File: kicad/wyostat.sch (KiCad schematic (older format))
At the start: 83 parts, among them J1 24 V AC IN, J10 Y2, J11 G, J12 W1, J13 USB_microAB, J14 W2, J15 Conn_Spare, J16 5V_SEL, J2 OUT1, J3 OUT2, J4 OUT3, J5 I2C_ext1, J6 RH, J7 RC, J8 C, J9 Y1, Q1 BTA204S, Q2 BTA204S, Q3 BTA204S, U1 MOC3063M, U2 MOC3063M, U3 MOC3063M, U4 Wemos-Lolin, U5 MAX17502FATB+T

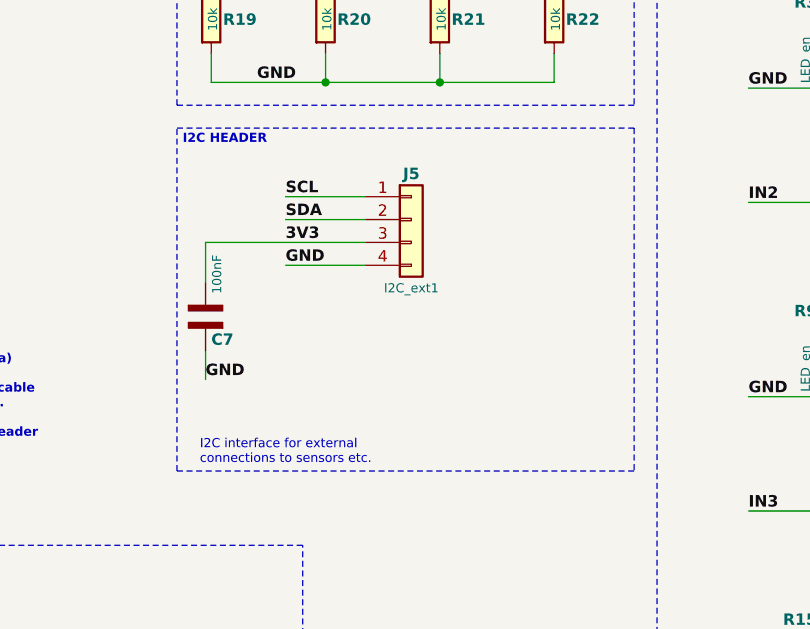
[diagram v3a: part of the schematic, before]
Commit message: added Sparkfun TMP102 footprint and PCB edges modified
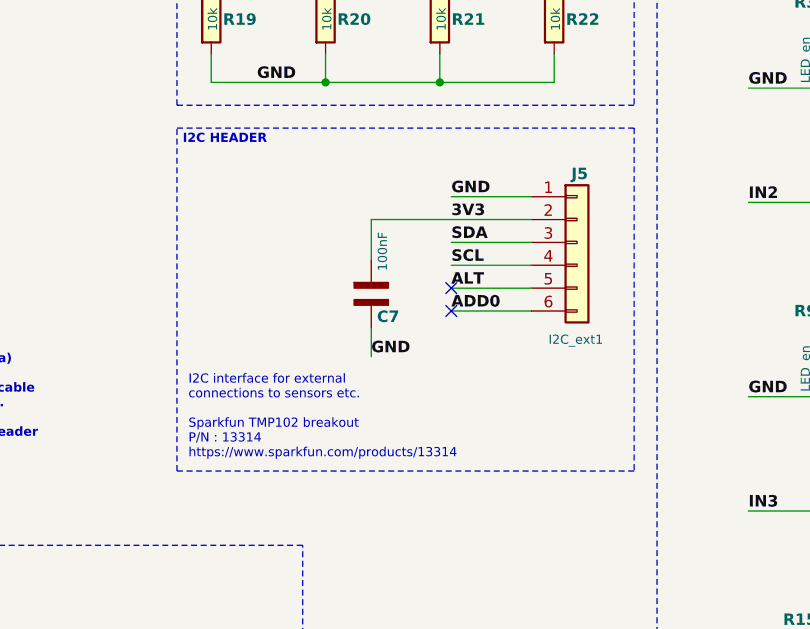
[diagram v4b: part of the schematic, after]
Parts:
- removed J5: I2C_ext1, wyostat_fp:Pin_Header_Straight_1x04, symbol wyostat:Conn_01x04
- added J5: I2C_ext1, wyostat_fp:Pin_Header_TMP102_1x06, symbol wyostat:Conn_01x06
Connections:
- net 3V3: now also J5.2 (Pin_2)
- net GND: now also J5.1 (Pin_1)
- net SCL: now also J5.4 (Pin_4)
- net SDA: now also J5.3 (Pin_3)
- new net ADD0: J5.6 (Pin_6)
- new net ALT: J5.5 (Pin_5)
- no-connect marks 15 -> 17
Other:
- note added: "I2C interface for external\nconnections to sensors etc.\n\nSparkfun TMP102 breakout\nP/N : 13314\nhttps://www.sparkfun.com/products/13314"
- note removed: "I2C interface for external\nconnections to sensors etc.\n"
- moved on the sheet: C7
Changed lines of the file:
@@
 Wire Notes Line
 	4825 2075 4825 575
-$Comp
-L wyostat:Conn_01x04 J5
-U 1 1 5AA95913
-P 5850 2575
-F 0 "J5" H 5850 2775 50  0000 C CNB
-F 1 "I2C_ext1" H 5850 2275 40  0000 C CNN
-F 2 "wyostat_fp:Pin_Header_Straight_1x04" H 5850 2575 50  0001 C CNN
-F 3 "~" H 5850 2575 50  0001 C CNN
-	1    5850 2575
-	1    0    0    -1
-$EndComp
-Text Label 5300 2575 0    50   ~ 10
+Text Label 6025 2675 0    50   ~ 10
 SDA
-Text Label 5300 2475 0    50   ~ 10
+Text Label 6025 2775 0    50   ~ 10
 SCL
-Text Label 5300 2675 0    50   ~ 10
+Text Label 6025 2575 0    50   ~ 10
 3V3
-Text Label 5300 2775 0    50   ~ 10
+Text Label 6025 2475 0    50   ~ 10
 GND
 Wire Wire Line
-	5650 2475 5300 2475
+	6375 2775 6025 2775
 Wire Wire Line
-	5300 2575 5650 2575
+	6025 2675 6375 2675
 Wire Wire Line
-	5300 2775 5650 2775
-Text Notes 4925 3650 0    40   ~ 0
-I2C interface for external\nconnections to sensors etc.\n
+	6025 2475 6375 2475
+Text Notes 4875 3625 0    40   ~ 0
+I2C interface for external\nconnections to sensors etc.\n\nSparkfun TMP102 breakout\nP/N : 13314\nhttps://www.sparkfun.com/products/13314
 Wire Notes Line
 	4825 2175 6825 2175
@@
 L wyostat:C_NP C7
 U 1 1 5AA95948
-P 4950 3000
-F 0 "C7" H 4975 2900 50  0000 L CNB
-F 1 "100nF" V 5000 3100 40  0000 L CNN
-F 2 "wyostat_fp:C_0805" H 4950 3000 60  0001 C CNN
-F 3 "" H 4950 3000 60  0000 C CNN
-	1    4950 3000
+P 5675 2900
+F 0 "C7" H 5700 2800 50  0000 L CNB
+F 1 "100nF" V 5725 3000 40  0000 L CNN
+F 2 "wyostat_fp:C_0805" H 5675 2900 60  0001 C CNN
+F 3 "" H 5675 2900 60  0000 C CNN
+	1    5675 2900
 	1    0    0    -1
 $EndComp
 Wire Wire Line
-	4950 2675 4950 2850
+	5675 2575 5675 2750
 Wire Wire Line
-	4950 2675 5650 2675
+	5675 2575 6375 2575
 Wire Wire Line
-	4950 3150 4950 3275
-Text Label 4950 3275 0    50   ~ 10
+	5675 3050 5675 3175
+Text Label 5675 3175 0    50   ~ 10
 GND
 Connection ~ 7675 1150
@@
 Text Notes 9475 5425 0    40   ~ 0
 Extra connection pads\nbrokenout to screw connector
+$Comp
+L wyostat:Conn_01x06 J5
+U 1 1 5ACA4E5A
+P 6575 2675
+F 0 "J5" H 6550 2975 50  0000 L CNB
+F 1 "I2C_ext1" H 6450 2250 40  0000 L CNN
+F 2 "wyostat_fp:Pin_Header_TMP102_1x06" H 6575 2675 50  0001 C CNN
+F 3 "~" H 6575 2675 50  0001 C CNN
+	1    6575 2675
+	1    0    0    -1
+$EndComp
+Wire Wire Line
+	6375 2875 6025 2875
+Wire Wire Line
+	6375 2975 6025 2975
+Text Label 6025 2875 0    50   ~ 10
+ALT
+Text Label 6025 2975 0    50   ~ 10
+ADD0
+NoConn ~ 6025 2875
+NoConn ~ 6025 2975
 $EndSCHEMATC

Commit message: prettified silk legend
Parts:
- C11: symbol wyostat:C_POL -> wyostat:C_NP
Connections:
- net 24Vac-H: now also C1.2 (-), C3.2 (-), C5.2 (-), R1.2, R13.2, R7.2; no longer C1.1 (+), C3.1 (+), C5.1 (+), R1.1, R13.1, R7.1
- net 3V3: now also C7.2 (-), S4.2, S4.4; no longer C7.1 (+), S4.1, S4.3
- net 40VDC: now also C11.2 (-); no longer C11.1 (+)
- net 5V_USB: now also L2.1; no longer L2.2
- net GND: now also C11.1 (+), C13.1 (+), C7.1 (+), JP1.2, JP2.2, JP3.2; no longer C11.2 (-), C13.2 (-), C7.2 (-), JP1.1, JP2.1, JP3.1
- net OUT1: now also R5.2; no longer R5.1
- net OUT2: now also R12.2; no longer R12.1
- net OUT3: now also R17.2; no longer R17.1
- net SS: now also C13.2 (-); no longer C13.1 (+)
- net SW_M: now also S4.1, S4.3; no longer S4.2, S4.4
- net USB+: now also L2.2; no longer L2.1
- net at Q1.3 (G), U1.4: now also R5.1; no longer R5.2
- net at U1.6: now also R1.1; no longer R1.2
- net at R3.1: now also JP1.1; no longer JP1.2
- net at Q2.3 (G), U2.4: now also R12.1; no longer R12.2
- net at U2.6: now also R7.1; no longer R7.2
- net at R9.1: now also JP2.1; no longer JP2.2
- net at Q3.3 (G), U3.4: now also R17.1; no longer R17.2
- net at U3.6: now also R13.1; no longer R13.2
- net at R15.1: now also JP3.1; no longer JP3.2
- net at R6.2: now also C1.1 (+); no longer C1.2 (-)
- net at R11.2: now also C3.1 (+); no longer C3.2 (-)
- net at R18.2: now also C5.1 (+); no longer C5.2 (-)
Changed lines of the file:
@@
 F 4 "Value" H 8775 1150 50  0001 C CNN "manf#"
 	1    8775 1150
-	0    1    1    0
+	0    -1   1    0
 $EndComp
 Text Label 10325 2025 0    50   ~ 10
@@
 F 4 "Value" H 8775 2500 50  0001 C CNN "manf#"
 	1    8775 2500
-	0    1    1    0
+	0    -1   1    0
 $EndComp
 Text Label 10325 3375 0    50   ~ 10
@@
 F 4 "Value" H 8775 3850 50  0001 C CNN "manf#"
 	1    8775 3850
-	0    1    1    0
+	0    -1   1    0
 $EndComp
 Text Label 10325 4725 0    50   ~ 10
@@
 U 1 1 5AA957F2
 P 6525 1125
-F 0 "S4" V 6600 1250 50  0000 L CNB
+F 0 "S4" V 6450 1250 50  0000 L CNB
 F 1 "SW-MODE" H 6525 1025 40  0000 C CNN
 F 2 "wyostat_fp:SW_SPST_FSM6JSMA" H 6525 1125 60  0001 C CNN
 F 3 "" H 6525 1125 60  0000 C CNN
 	1    6525 1125
-	0    1    1    0
+	0    1    -1   0
 $EndComp
 Wire Wire Line
@@
 P 5675 2900
 F 0 "C7" H 5700 2800 50  0000 L CNB
-F 1 "100nF" V 5725 3000 40  0000 L CNN
+F 1 "100nF" V 5625 2625 40  0000 L CNN
 F 2 "wyostat_fp:C_0805" H 5675 2900 60  0001 C CNN
 F 3 "" H 5675 2900 60  0000 C CNN
 	1    5675 2900
-	1    0    0    -1
+	1    0    0    1
 $EndComp
 Wire Wire Line
@@
 P 7675 1900
 F 0 "JP1" V 7675 1875 50  0000 R CNB
-F 1 "LED_en" H 7800 2000 40  0000 R CNN
+F 1 "LED_en" H 7775 2000 40  0000 R CNN
 F 2 "wyostat_fp:R_0805" H 7675 1900 50  0001 C CNN
 F 3 "" H 7675 1900 50  0001 C CNN
 	1    7675 1900
-	0    -1   -1   0
+	0    -1   1    0
 $EndComp
 Wire Wire Line
@@
 P 7675 3250
 F 0 "JP2" V 7675 3225 50  0000 R CNB
-F 1 "LED_en" H 7800 3350 40  0000 R CNN
+F 1 "LED_en" H 7750 3350 40  0000 R CNN
 F 2 "wyostat_fp:R_0805" H 7675 3250 50  0001 C CNN
 F 3 "" H 7675 3250 50  0001 C CNN
 	1    7675 3250
-	0    -1   -1   0
+	0    -1   1    0
 $EndComp
 Connection ~ 7675 3350
@@
 P 7675 4600
 F 0 "JP3" V 7675 4575 50  0000 R CNB
-F 1 "LED_en" H 7800 4700 40  0000 R CNN
+F 1 "LED_en" H 7750 4700 40  0000 R CNN
 F 2 "wyostat_fp:R_0805" H 7675 4600 50  0001 C CNN
 F 3 "" H 7675 4600 50  0001 C CNN
 	1    7675 4600
-	0    -1   -1   0
+	0    -1   1    0
 $EndComp
 Connection ~ 7675 4700
@@
 F 5 "-" V 8850 1750 30  0001 C CNN "DNP"
 	1    8775 1750
-	-1   0    0    1
+	-1   0    0    -1
 $EndComp
 Wire Wire Line
@@
 F 5 "-" V 8850 3150 30  0001 C CNN "DNP"
 	1    8775 3150
-	-1   0    0    1
+	-1   0    0    -1
 $EndComp
 $Comp
@@
 F 5 "-" V 8850 4450 30  0001 C CNN "DNP"
 	1    8775 4450
-	-1   0    0    1
+	-1   0    0    -1
 $EndComp
 $Comp
@@
 U 1 1 5ADF342F
 P 9900 1400
-F 0 "C1" H 9925 1500 50  0000 L CNB
-F 1 "10nF,120V" H 9925 1300 40  0000 L CNN
+F 0 "C1" H 9925 1300 50  0000 L CNB
+F 1 "10nF,120V" H 9925 1500 40  0000 L CNN
 F 2 "wyostat_fp:C_1210" H 9900 1400 60  0001 C CNN
 F 3 "" H 9900 1400 60  0000 C CNN
 	1    9900 1400
-	1    0    0    -1
+	1    0    0    1
 $EndComp
 $Comp
@@
 U 1 1 5AE133E2
 P 9900 2750
-F 0 "C3" H 9925 2850 50  0000 L CNB
-F 1 "10nF,120V" H 9925 2650 40  0000 L CNN
+F 0 "C3" H 9925 2650 50  0000 L CNB
+F 1 "10nF,120V" H 9925 2850 40  0000 L CNN
 F 2 "wyostat_fp:C_1210" H 9900 2750 60  0001 C CNN
 F 3 "" H 9900 2750 60  0000 C CNN
 	1    9900 2750
-	1    0    0    -1
+	1    0    0    1
 $EndComp
 $Comp
@@
 U 1 1 5AE1E610
 P 9900 4100
-F 0 "C5" H 9925 4200 50  0000 L CNB
-F 1 "10nF,120V" H 9925 4000 40  0000 L CNN
+F 0 "C5" H 9925 4000 50  0000 L CNB
+F 1 "10nF,120V" H 9925 4200 40  0000 L CNN
 F 2 "wyostat_fp:C_1210" H 9900 4100 60  0001 C CNN
 F 3 "" H 9900 4100 60  0000 C CNN
 	1    9900 4100
-	1    0    0    -1
+	1    0    0    1
 $EndComp
 $Comp
@@
 $EndComp
 $Comp
-L wyostat:C_POL C11
+L wyostat:C_NP C11
 U 1 1 5AAA90E7
 P 2525 7075
-F 0 "C11" H 2550 6975 50  0000 L CNB
-F 1 "2.2uF,50V" V 2575 7200 40  0000 L CNN
+F 0 "C11" H 2550 7175 50  0000 L CNB
+F 1 "2.2uF,50V" V 2575 6700 40  0000 L CNN
 F 2 "wyostat_fp:C_0805" H 2525 7075 60  0001 C CNN
 F 3 "" H 2525 7075 60  0000 C CNN
 	1    2525 7075
-	1    0    0    -1
+	1    0    0    1
 $EndComp
 Wire Wire Line
@@
 U 1 1 5AB290FF
 P 2975 7075
-F 0 "C13" H 3000 6975 50  0000 L CNB
-F 1 "3.3nF" V 3025 7150 40  0000 L CNN
+F 0 "C13" H 3000 7175 50  0000 L CNB
+F 1 "3.3nF" V 2925 6825 40  0000 L CNN
 F 2 "wyostat_fp:C_0805" H 2975 7075 60  0001 C CNN
 F 3 "" H 2975 7075 60  0000 C CNN
 	1    2975 7075
-	1    0    0    -1
+	1    0    0    1
 $EndComp
 Wire Wire Line
@@
 GND
 $Comp
-L wyostat:GND #PWR02
+L wyostat:GND #PWR?
 U 1 1 5ABB9ABE
 P 2075 7600
-F 0 "#PWR02" H 2075 7350 50  0001 C CNN
+F 0 "#PWR?" H 2075 7350 50  0001 C CNN
 F 1 "GND" H 2175 7650 40  0000 C CNN
 F 2 "" H 2075 7600 50  0001 C CNN
@@
 $EndComp
 $Comp
-L wyostat:GNDREF #PWR03
+L wyostat:GNDREF #PWR?
 U 1 1 5ABDBAC8
 P 5100 7500
-F 0 "#PWR03" H 5100 7250 50  0001 C CNN
+F 0 "#PWR?" H 5100 7250 50  0001 C CNN
 F 1 "GNDREF" H 5225 7500 40  0000 C CNN
 F 2 "" H 5100 7500 50  0001 C CNN
@@
 AC-DC POWER SUPPLY
 $Comp
-L wyostat:GND #PWR01
+L wyostat:GND #PWR?
 U 1 1 5ADAE2BA
 P 3725 7375
-F 0 "#PWR01" H 3725 7125 50  0001 C CNN
+F 0 "#PWR?" H 3725 7125 50  0001 C CNN
 F 1 "GND" H 3825 7375 40  0000 C CNN
 F 2 "" H 3725 7375 50  0001 C CNN
@@
 NoConn ~ 1275 1250
 $Comp
-L wyostat:PWR_FLAG #FLG03
+L wyostat:PWR_FLAG #FLG?
 U 1 1 5AECC9F1
 P 4975 6225
-F 0 "#FLG03" H 4975 6300 50  0001 C CNN
+F 0 "#FLG?" H 4975 6300 50  0001 C CNN
 F 1 "PWR_FLAG" H 4975 6375 40  0000 C CNN
 F 2 "" H 4975 6225 50  0001 C CNN
@@
 	4975 6225 4975 6275
 $Comp
-L wyostat:PWR_FLAG #FLG01
+L wyostat:PWR_FLAG #FLG?
 U 1 1 5AEE02D5
 P 2475 775
-F 0 "#FLG01" H 2475 850 50  0001 C CNN
+F 0 "#FLG?" H 2475 850 50  0001 C CNN
 F 1 "PWR_FLAG" H 2475 925 40  0000 C CNN
 F 2 "" H 2475 775 50  0001 C CNN
@@
 Connection ~ 2475 825
 $Comp
-L wyostat:PWR_FLAG #FLG02
+L wyostat:PWR_FLAG #FLG?
 U 1 1 5AEF4507
 P 2775 775
-F 0 "#FLG02" H 2775 850 50  0001 C CNN
+F 0 "#FLG?" H 2775 850 50  0001 C CNN
 F 1 "PWR_FLAG" H 2775 925 40  0000 C CNN
 F 2 "" H 2775 775 50  0001 C CNN
@@
 U 1 1 5AE9DEF9
 P 2750 7475
-F 0 "JP4" V 2705 7552 50  0000 L CNB
-F 1 "GND" V 2795 7552 40  0000 L CNN
+F 0 "JP4" V 2775 7550 50  0000 L CNB
+F 1 "GND" V 2700 7550 40  0000 L CNN
 F 2 "wyostat_fp:LED_0402" H 2750 7475 50  0001 C CNN
 F 3 "" H 2750 7475 50  0001 C CNN
 	1    2750 7475
-	0    1    1    0
+	0    1    -1   0
 $EndComp
 Wire Wire Line
@@
 	1    0    0    -1
 $EndComp
-Wire Wire Line
-	2675 7550 2675 7400
-Wire Wire Line
-	2675 7400 2750 7325
-Wire Wire Line
-	2675 7550 2750 7625
 Text Label 675  6575 0    50   ~ 10
 24Vac-H
@@
 F 4 "Value" H 2950 4425 50  0001 C CNN "manf#"
 	1    2950 4425
-	1    0    0    -1
+	-1   0    0    -1
 $EndComp
 Wire Wire Line
@@
 	3950 4850 3075 4850
 $Comp
-L power:GND #PWR0101
+L power:GND #PWR?
 U 1 1 5AAF3C1A
 P 1600 5625
-F 0 "#PWR0101" H 1600 5375 50  0001 C CNN
+F 0 "#PWR?" H 1600 5375 50  0001 C CNN
 F 1 "GND" H 1525 5625 40  0000 C CNN
 F 2 "" H 1600 5625 50  0001 C CNN
@@
 $EndComp
 $Comp
-L power:GND #PWR0102
+L power:GND #PWR?
 U 1 1 5AAF3C20
 P 1750 5625
-F 0 "#PWR0102" H 1750 5375 50  0001 C CNN
+F 0 "#PWR?" H 1750 5375 50  0001 C CNN
 F 1 "GND" H 1825 5625 40  0000 C CNN
 F 2 "" H 1750 5625 50  0001 C CNN
@@
 $EndComp
 $Comp
-L power:GND #PWR0103
+L power:GND #PWR?
 U 1 1 5AAF3C26
 P 2025 5625
-F 0 "#PWR0103" H 2025 5375 50  0001 C CNN
+F 0 "#PWR?" H 2025 5375 50  0001 C CNN
 F 1 "GND" H 2100 5625 40  0000 C CNN
 F 2 "" H 2025 5625 50  0001 C CNN
@@
 $EndComp
 $Comp
-L power:GND #PWR0104
+L power:GND #PWR?
 U 1 1 5AAF3C2C
 P 3325 5625
-F 0 "#PWR0104" H 3325 5375 50  0001 C CNN
+F 0 "#PWR?" H 3325 5375 50  0001 C CNN
 F 1 "GND" H 3400 5625 40  0000 C CNN
 F 2 "" H 3325 5625 50  0001 C CNN
@@
 NoConn ~ 6025 2875
 NoConn ~ 6025 2975
+Wire Wire Line
+	2675 7550 2750 7625
+Wire Wire Line
+	2675 7400 2750 7325
+Wire Wire Line
+	2675 7550 2675 7400
 $EndSCHEMATC
